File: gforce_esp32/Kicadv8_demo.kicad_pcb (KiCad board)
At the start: 8 copper layers, 160 x 160 mm, 65 parts, among them J1 USB_C_Receptacle, SW1 TL3215AF160BQ, SW2 TL3215AF160RQ, U1 ESP32-S3-MINI-1U, U2 AP2112K-3.3, U3 LIS3DH

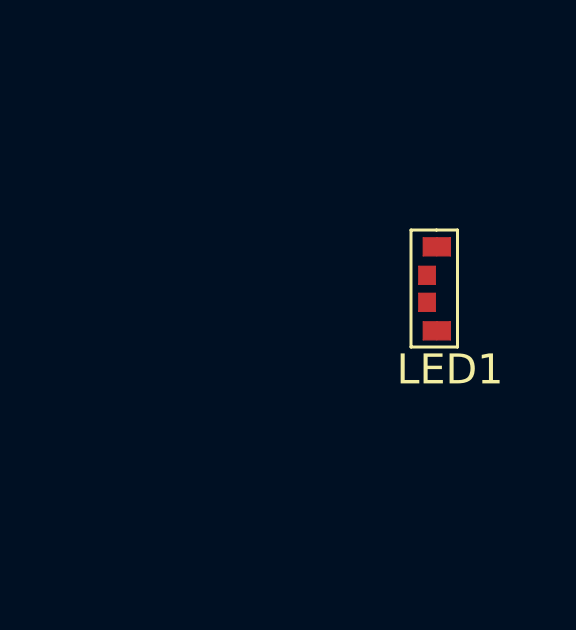
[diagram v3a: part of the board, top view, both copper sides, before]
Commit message: SCHEMATIC LEDS MAPPED. FAB NOTES ADDED
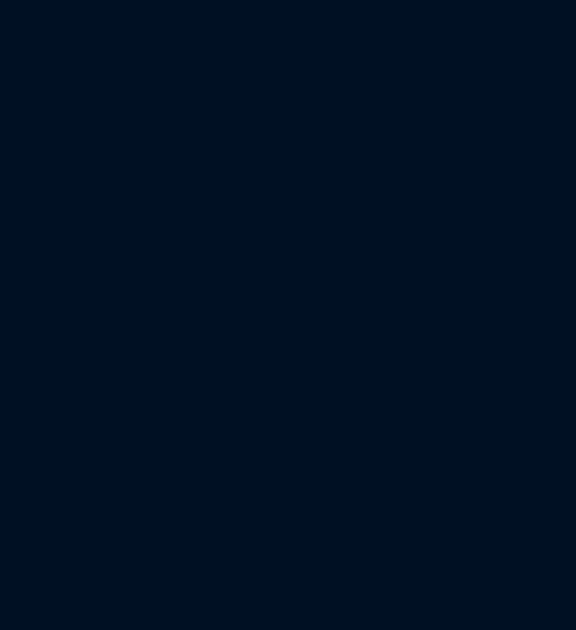
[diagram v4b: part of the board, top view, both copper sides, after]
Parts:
- removed LED1: ~, B3DQ3BRG_SMT:B3DQ3BRG
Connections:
- D1 pad 1: unconnected-(D1-VDD-Pad1) -> +5V
- D1 pad 2: unconnected-(D1-DOUT-Pad2) -> Net-(D1-DOUT)
- D1 pad 3: unconnected-(D1-VSS-Pad3) -> GND
- D1 pad 4: unconnected-(D1-DIN-Pad4) -> /NEOPXL
- D10 pad 1: unconnected-(D10-VDD-Pad1) -> +5V
- D10 pad 2: unconnected-(D10-DOUT-Pad2) -> Net-(D10-DOUT)
- D10 pad 3: unconnected-(D10-VSS-Pad3) -> GND
- D10 pad 4: unconnected-(D10-DIN-Pad4) -> Net-(D10-DIN)
- D11 pad 1: unconnected-(D11-VDD-Pad1) -> +5V
- D11 pad 2: unconnected-(D11-DOUT-Pad2) -> Net-(D11-DOUT)
- D11 pad 3: unconnected-(D11-VSS-Pad3) -> GND
- D11 pad 4: unconnected-(D11-DIN-Pad4) -> Net-(D10-DOUT)
- D12 pad 1: unconnected-(D12-VDD-Pad1) -> +5V
- D12 pad 2: unconnected-(D12-DOUT-Pad2) -> Net-(D12-DOUT)
- D12 pad 3: unconnected-(D12-VSS-Pad3) -> GND
- D12 pad 4: unconnected-(D12-DIN-Pad4) -> Net-(D11-DOUT)
- D13 pad 1: unconnected-(D13-VDD-Pad1) -> +5V
- D13 pad 2: unconnected-(D13-DOUT-Pad2) -> Net-(D13-DOUT)
- D13 pad 3: unconnected-(D13-VSS-Pad3) -> GND
- D13 pad 4: unconnected-(D13-DIN-Pad4) -> Net-(D12-DOUT)
- D14 pad 1: unconnected-(D14-VDD-Pad1) -> +5V
- D14 pad 2: unconnected-(D14-DOUT-Pad2) -> Net-(D14-DOUT)
- D14 pad 3: unconnected-(D14-VSS-Pad3) -> GND
- D14 pad 4: unconnected-(D14-DIN-Pad4) -> Net-(D13-DOUT)
- D15 pad 1: unconnected-(D15-VDD-Pad1) -> +5V
- D15 pad 2: unconnected-(D15-DOUT-Pad2) -> Net-(D15-DOUT)
- D15 pad 3: unconnected-(D15-VSS-Pad3) -> GND
- D15 pad 4: unconnected-(D15-DIN-Pad4) -> Net-(D14-DOUT)
- D16 pad 1: unconnected-(D16-VDD-Pad1) -> +5V
- D16 pad 2: unconnected-(D16-DOUT-Pad2) -> Net-(D16-DOUT)
- D16 pad 3: unconnected-(D16-VSS-Pad3) -> GND
- D16 pad 4: unconnected-(D16-DIN-Pad4) -> Net-(D15-DOUT)
- D17 pad 1: unconnected-(D17-VDD-Pad1) -> +5V
- D17 pad 2: unconnected-(D17-DOUT-Pad2) -> Net-(D17-DOUT)
- D17 pad 3: unconnected-(D17-VSS-Pad3) -> GND
- D17 pad 4: unconnected-(D17-DIN-Pad4) -> Net-(D16-DOUT)
- D18 pad 1: unconnected-(D18-VDD-Pad1) -> +5V
- D18 pad 2: unconnected-(D18-DOUT-Pad2) -> Net-(D18-DOUT)
- D18 pad 3: unconnected-(D18-VSS-Pad3) -> GND
- D18 pad 4: unconnected-(D18-DIN-Pad4) -> Net-(D17-DOUT)
- D19 pad 1: unconnected-(D19-VDD-Pad1) -> +5V
- D19 pad 2: unconnected-(D19-DOUT-Pad2) -> Net-(D19-DOUT)
- D19 pad 3: unconnected-(D19-VSS-Pad3) -> GND
- D19 pad 4: unconnected-(D19-DIN-Pad4) -> Net-(D18-DOUT)
- D2 pad 1: unconnected-(D2-VDD-Pad1) -> +5V
- D2 pad 2: unconnected-(D2-DOUT-Pad2) -> Net-(D2-DOUT)
- D2 pad 3: unconnected-(D2-VSS-Pad3) -> GND
- D2 pad 4: unconnected-(D2-DIN-Pad4) -> Net-(D1-DOUT)
- D20 pad 1: unconnected-(D20-VDD-Pad1) -> +5V
- D20 pad 2: unconnected-(D20-DOUT-Pad2) -> Net-(D20-DOUT)
- D20 pad 3: unconnected-(D20-VSS-Pad3) -> GND
- D20 pad 4: unconnected-(D20-DIN-Pad4) -> Net-(D19-DOUT)
- D21 pad 1: unconnected-(D21-VDD-Pad1) -> +5V
- D21 pad 2: unconnected-(D21-DOUT-Pad2) -> Net-(D21-DOUT)
- D21 pad 3: unconnected-(D21-VSS-Pad3) -> GND
- D21 pad 4: unconnected-(D21-DIN-Pad4) -> Net-(D20-DOUT)
- D22 pad 1: unconnected-(D22-VDD-Pad1) -> +5V
- D22 pad 2: unconnected-(D22-DOUT-Pad2) -> Net-(D22-DOUT)
- D22 pad 3: unconnected-(D22-VSS-Pad3) -> GND
- D22 pad 4: unconnected-(D22-DIN-Pad4) -> Net-(D21-DOUT)
- D23 pad 1: unconnected-(D23-VDD-Pad1) -> +5V
- D23 pad 2: unconnected-(D23-DOUT-Pad2) -> Net-(D23-DOUT)
- D23 pad 3: unconnected-(D23-VSS-Pad3) -> GND
- D23 pad 4: unconnected-(D23-DIN-Pad4) -> Net-(D22-DOUT)
- D24 pad 1: unconnected-(D24-VDD-Pad1) -> +5V
- D24 pad 2: unconnected-(D24-DOUT-Pad2) -> Net-(D24-DOUT)
- D24 pad 3: unconnected-(D24-VSS-Pad3) -> GND
- D24 pad 4: unconnected-(D24-DIN-Pad4) -> Net-(D23-DOUT)
- D25 pad 1: unconnected-(D25-VDD-Pad1) -> +5V
- D25 pad 2: unconnected-(D25-DOUT-Pad2) -> Net-(D25-DOUT)
- D25 pad 3: unconnected-(D25-VSS-Pad3) -> GND
- D25 pad 4: unconnected-(D25-DIN-Pad4) -> Net-(D24-DOUT)
- D26 pad 1: unconnected-(D26-VDD-Pad1) -> +5V
- D26 pad 2: unconnected-(D26-DOUT-Pad2) -> Net-(D26-DOUT)
- D26 pad 3: unconnected-(D26-VSS-Pad3) -> GND
- D26 pad 4: unconnected-(D26-DIN-Pad4) -> Net-(D25-DOUT)
- D27 pad 1: unconnected-(D27-VDD-Pad1) -> +5V
- D27 pad 2: unconnected-(D27-DOUT-Pad2) -> Net-(D27-DOUT)
- D27 pad 3: unconnected-(D27-VSS-Pad3) -> GND
- D27 pad 4: unconnected-(D27-DIN-Pad4) -> Net-(D26-DOUT)
- D28 pad 1: unconnected-(D28-VDD-Pad1) -> +5V
- D28 pad 2: unconnected-(D28-DOUT-Pad2) -> Net-(D28-DOUT)
- D28 pad 3: unconnected-(D28-VSS-Pad3) -> GND
- D28 pad 4: unconnected-(D28-DIN-Pad4) -> Net-(D27-DOUT)
- D29 pad 1: unconnected-(D29-VDD-Pad1) -> +5V
- D29 pad 2: unconnected-(D29-DOUT-Pad2) -> Net-(D29-DOUT)
- D29 pad 3: unconnected-(D29-VSS-Pad3) -> GND
- D29 pad 4: unconnected-(D29-DIN-Pad4) -> Net-(D28-DOUT)
- D3 pad 1: unconnected-(D3-VDD-Pad1) -> +5V
- D3 pad 2: unconnected-(D3-DOUT-Pad2) -> Net-(D3-DOUT)
- D3 pad 3: unconnected-(D3-VSS-Pad3) -> GND
- D3 pad 4: unconnected-(D3-DIN-Pad4) -> Net-(D2-DOUT)
- D30 pad 1: unconnected-(D30-VDD-Pad1) -> +5V
- D30 pad 2: unconnected-(D30-DOUT-Pad2) -> Net-(D30-DOUT)
- D30 pad 3: unconnected-(D30-VSS-Pad3) -> GND
- D30 pad 4: unconnected-(D30-DIN-Pad4) -> Net-(D29-DOUT)
- D31 pad 1: unconnected-(D31-VDD-Pad1) -> +5V
- D31 pad 2: unconnected-(D31-DOUT-Pad2) -> Net-(D31-DOUT)
- D31 pad 3: unconnected-(D31-VSS-Pad3) -> GND
- D31 pad 4: unconnected-(D31-DIN-Pad4) -> Net-(D30-DOUT)
- D32 pad 1: unconnected-(D32-VDD-Pad1) -> +5V
- D32 pad 2: unconnected-(D32-DOUT-Pad2) -> Net-(D32-DOUT)
- D32 pad 3: unconnected-(D32-VSS-Pad3) -> GND
- D32 pad 4: unconnected-(D32-DIN-Pad4) -> Net-(D31-DOUT)
- D33 pad 1: unconnected-(D33-VDD-Pad1) -> +5V
- D33 pad 2: unconnected-(D33-DOUT-Pad2) -> Net-(D33-DOUT)
- D33 pad 3: unconnected-(D33-VSS-Pad3) -> GND
- D33 pad 4: unconnected-(D33-DIN-Pad4) -> Net-(D32-DOUT)
- D34 pad 1: unconnected-(D34-VDD-Pad1) -> +5V
- D34 pad 2: unconnected-(D34-DOUT-Pad2) -> Net-(D34-DOUT)
- D34 pad 3: unconnected-(D34-VSS-Pad3) -> GND
- D34 pad 4: unconnected-(D34-DIN-Pad4) -> Net-(D33-DOUT)
- D35 pad 1: unconnected-(D35-VDD-Pad1) -> +5V
- D35 pad 2: unconnected-(D35-DOUT-Pad2) -> Net-(D35-DOUT)
- D35 pad 3: unconnected-(D35-VSS-Pad3) -> GND
- D35 pad 4: unconnected-(D35-DIN-Pad4) -> Net-(D34-DOUT)
- D36 pad 1: unconnected-(D36-VDD-Pad1) -> +5V
- D36 pad 2: unconnected-(D36-DOUT-Pad2) -> Net-(D36-DOUT)
- D36 pad 3: unconnected-(D36-VSS-Pad3) -> GND
- D36 pad 4: unconnected-(D36-DIN-Pad4) -> Net-(D35-DOUT)
- D37 pad 1: unconnected-(D37-VDD-Pad1) -> +5V
- D37 pad 2: unconnected-(D37-DOUT-Pad2) -> Net-(D37-DOUT)
- D37 pad 3: unconnected-(D37-VSS-Pad3) -> GND
- D37 pad 4: unconnected-(D37-DIN-Pad4) -> Net-(D36-DOUT)
- D38 pad 1: unconnected-(D38-VDD-Pad1) -> +5V
- D38 pad 2: unconnected-(D38-DOUT-Pad2) -> Net-(D38-DOUT)
- D38 pad 3: unconnected-(D38-VSS-Pad3) -> GND
- D38 pad 4: unconnected-(D38-DIN-Pad4) -> Net-(D37-DOUT)
- D39 pad 1: unconnected-(D39-VDD-Pad1) -> +5V
- D39 pad 2: unconnected-(D39-DOUT-Pad2) -> Net-(D39-DOUT)
- D39 pad 3: unconnected-(D39-VSS-Pad3) -> GND
- D39 pad 4: unconnected-(D39-DIN-Pad4) -> Net-(D38-DOUT)
- D4 pad 1: unconnected-(D4-VDD-Pad1) -> +5V
- D4 pad 2: unconnected-(D4-DOUT-Pad2) -> Net-(D4-DOUT)
- D4 pad 3: unconnected-(D4-VSS-Pad3) -> GND
- D4 pad 4: unconnected-(D4-DIN-Pad4) -> Net-(D3-DOUT)
- D40 pad 1: unconnected-(D40-VDD-Pad1) -> +5V
- D40 pad 3: unconnected-(D40-VSS-Pad3) -> GND
- D40 pad 4: unconnected-(D40-DIN-Pad4) -> Net-(D39-DOUT)
- D5 pad 1: unconnected-(D5-VDD-Pad1) -> +5V
- D5 pad 2: unconnected-(D5-DOUT-Pad2) -> Net-(D5-DOUT)
- D5 pad 3: unconnected-(D5-VSS-Pad3) -> GND
- D5 pad 4: unconnected-(D5-DIN-Pad4) -> Net-(D4-DOUT)
- D6 pad 1: unconnected-(D6-VDD-Pad1) -> +5V
- D6 pad 2: unconnected-(D6-DOUT-Pad2) -> Net-(D6-DOUT)
- D6 pad 3: unconnected-(D6-VSS-Pad3) -> GND
- D6 pad 4: unconnected-(D6-DIN-Pad4) -> Net-(D5-DOUT)
- D7 pad 1: unconnected-(D7-VDD-Pad1) -> +5V
- D7 pad 2: unconnected-(D7-DOUT-Pad2) -> Net-(D7-DOUT)
- D7 pad 3: unconnected-(D7-VSS-Pad3) -> GND
- D7 pad 4: unconnected-(D7-DIN-Pad4) -> Net-(D6-DOUT)
- D8 pad 1: unconnected-(D8-VDD-Pad1) -> +5V
- D8 pad 2: unconnected-(D8-DOUT-Pad2) -> Net-(D8-DOUT)
- D8 pad 3: unconnected-(D8-VSS-Pad3) -> GND
- D8 pad 4: unconnected-(D8-DIN-Pad4) -> Net-(D7-DOUT)
- D9 pad 1: unconnected-(D9-VDD-Pad1) -> +5V
- D9 pad 2: unconnected-(D9-DOUT-Pad2) -> Net-(D10-DIN)
- D9 pad 3: unconnected-(D9-VSS-Pad3) -> GND
- D9 pad 4: unconnected-(D9-DIN-Pad4) -> Net-(D8-DOUT)
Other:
- board text added: "BOARD STACKUP"
- board text added: "FR4-TG 150-160 IMMERSION GOLD(ENIG) NO LEAD THICKNESS 1.6MM GREEN SOLDER MASK WHITE SILKSCREEN TENTING VIAS ALL LAYERS 1 OZ CU"
- board text added: "LAYER 1 SIGNAL1"
- board text added: "LAYER 2 GND1"
- board text added: "LAYER 3 5VDC"
- board text added: "LAYER 4 GND2"
- board text added: "LAYER 5 3.3VDC"
- board text added: "LAYER 6 GND3"
- board text added: "LAYER 7 SIGNAL2"
- board text added: "LAYER 8 GND4"

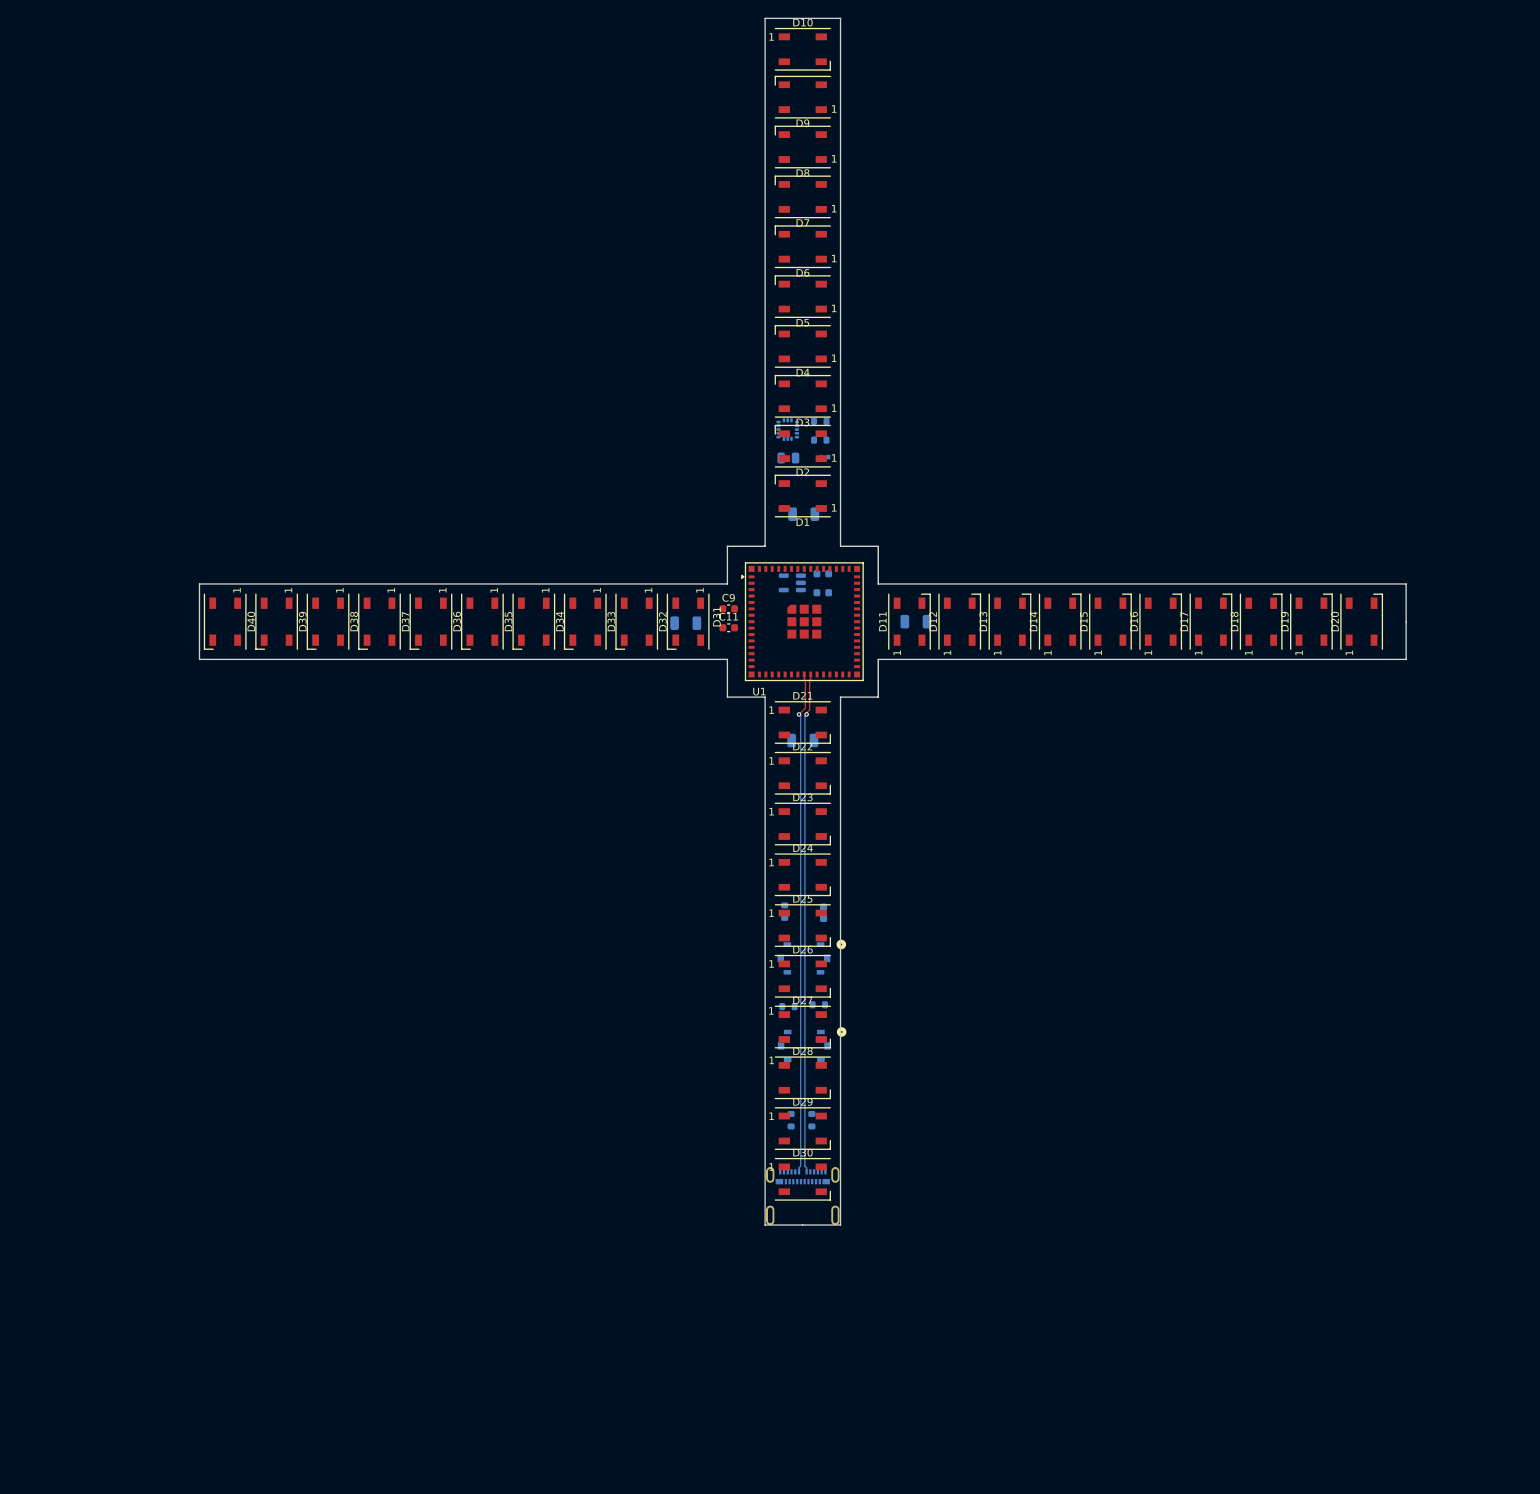
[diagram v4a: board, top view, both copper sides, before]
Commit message: some net pours and routing
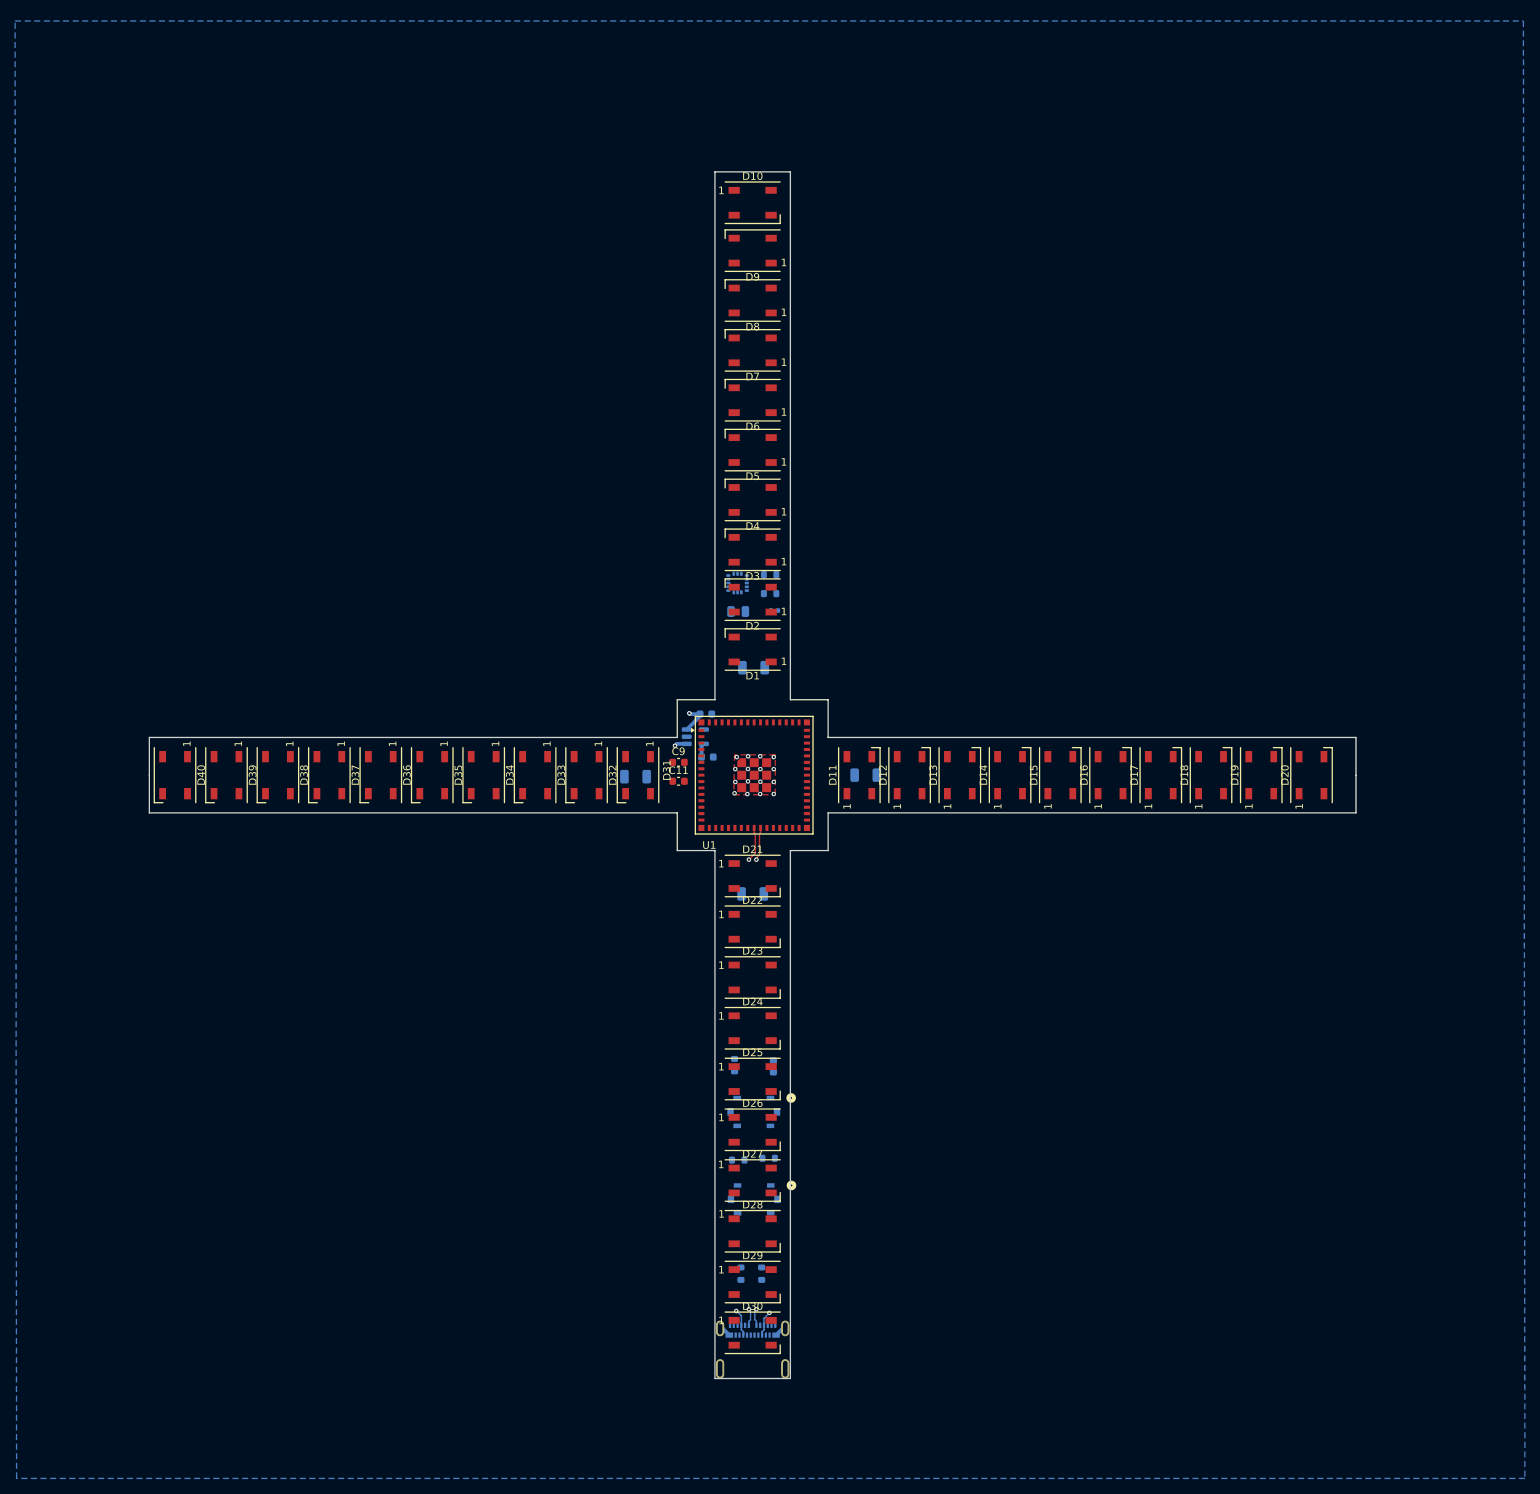
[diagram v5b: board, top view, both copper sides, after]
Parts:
- moved C6 26.6 mm to (131.8, 117.6), turned to 0 degrees
- moved C1 24.2 mm to (131.6, 111.9), turned to 0 degrees
- moved U2 24.1 mm to (130.2, 114.9), turned to 0 degrees
- moved D26 21.4 mm to (137.8, 167.0)
- moved C11 21.4 mm to (128.0, 120.8)
- moved C5 21.4 mm to (122.3, 120.2)
- moved C7 21.4 mm to (140.7, 98.2)
- moved D1 21.4 mm to (137.8, 103.3)
- moved D2 21.4 mm to (137.8, 96.7)
- moved D21 21.4 mm to (137.8, 133.4)
- moved D23 21.4 mm to (137.8, 146.8)
- moved D3 21.4 mm to (137.8, 90.1)
- moved R5 21.4 mm to (139.9, 170.8)
- moved D7 21.4 mm to (137.8, 63.7)
- moved D8 21.4 mm to (137.8, 57.1)
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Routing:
- net +5V: track 0.00 -> 12.9 mm, vias 0 -> 4
- net GND: track 0.00 -> 3.04 mm, vias 0 -> 16
- net +3V3: track 0.00 -> 1.88 mm
- net /D-: track 66.5 -> 66.8 mm, vias 1 -> 2
- net /D+: track 66.4 -> 66.5 mm, vias 1 -> 2
- added copper zone on In2.Cu, net +5V
- added copper zone on B.Cu, net GND
- added copper zone on F.Cu, net GND
- added copper zone on In1.Cu, net GND
- added copper zone on In3.Cu, net GND
- added copper zone on In5.Cu, net GND
